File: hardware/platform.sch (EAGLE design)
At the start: 24 parts, among them CN1 MiniB USB, IC1 ATMEGA32U4-AU, X3 16MHz

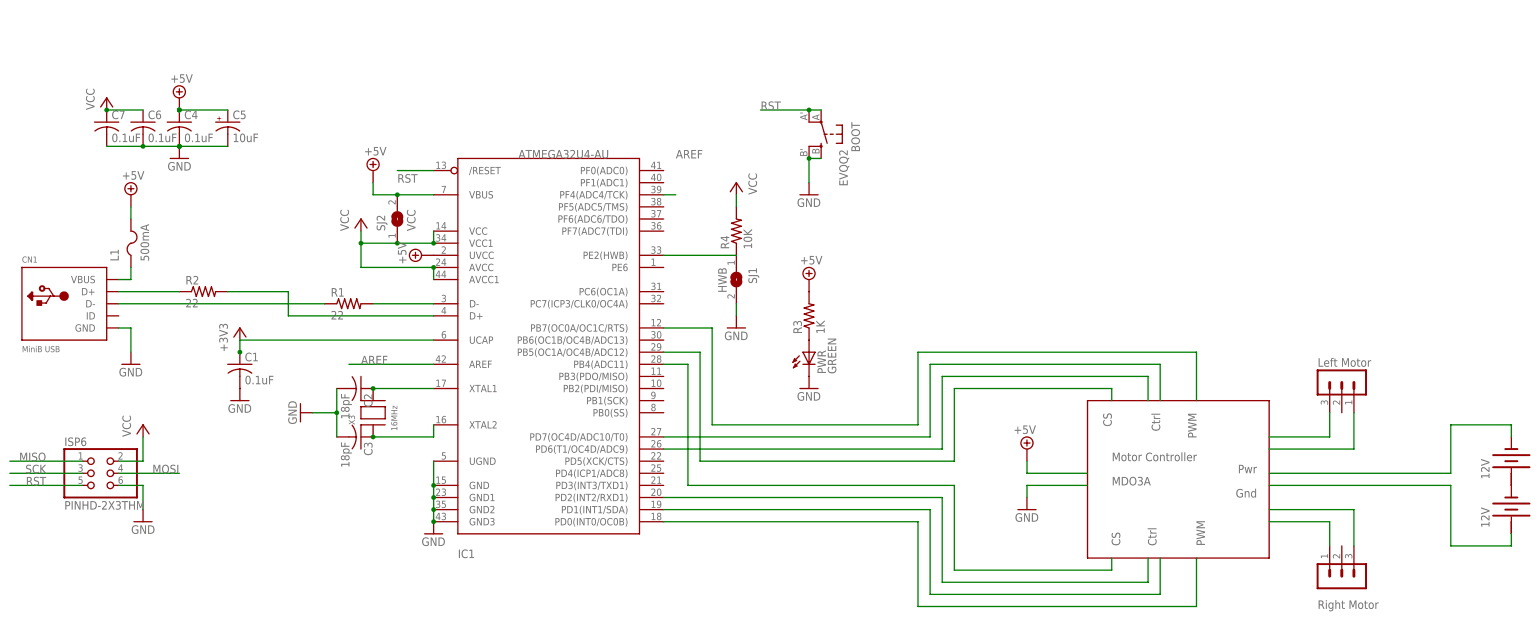
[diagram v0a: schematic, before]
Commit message: Added sonar sensors
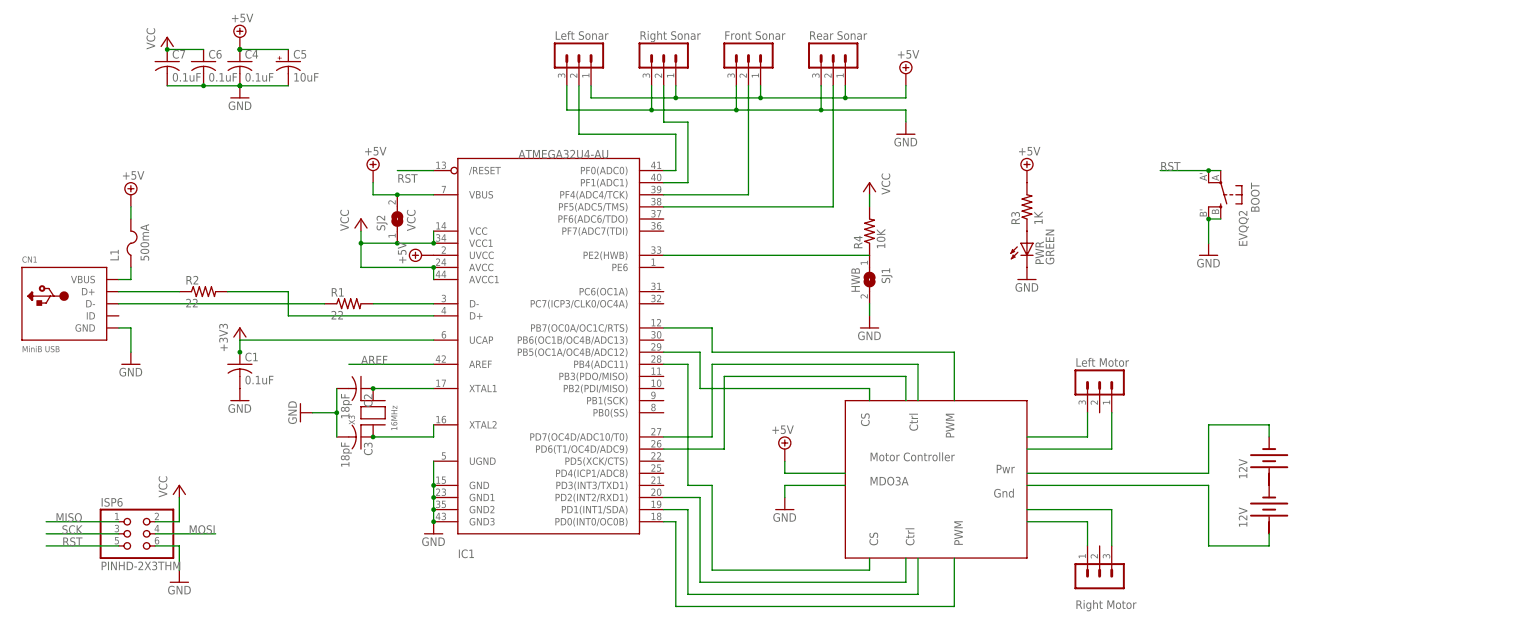
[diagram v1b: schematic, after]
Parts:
- added SV3: Left Sonar, con-lstb:MA03-1
- added SV4: Right Sonar, con-lstb:MA03-1
- added SV5: Front Sonar, con-lstb:MA03-1
- added SV6: Rear Sonar, con-lstb:MA03-1
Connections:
- new net N$23: IC1.PF0(ADC0), SV3.2
- new net N$24: IC1.PF1(ADC1), SV4.2
- new net N$25: IC1.PF5(ADC5/TMS), SV6.2
- net +5V: now also SV3.1, SV4.1, SV5.1, SV6.1
- net GND: now also SV3.3, SV4.3, SV5.3, SV6.3
- net PF4: now also SV5.2
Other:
- moved on the sheet: BOOT, C4, C5, C6, C7, ISP6, PWR, R3, R4, SJ1
